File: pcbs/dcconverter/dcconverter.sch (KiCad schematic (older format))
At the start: 41 parts, among them IC1 NCP7805TG, J1 190-9991, J2 766-6629, J3 146-8335, J4 766-6604, J5 766-6604, Q1 NGTB40N120FL2WG, Q10 398-433, Q2 FQP47P06, Q3 2SK3747-1E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

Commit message: Cleanup Symbol Library
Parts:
- IC1: symbol SamacSys_Parts:NCP7805TG -> Custom:NCP7805TG
- L1: symbol dcconverter:2phase_inductor -> Custom:2phase_inductor
- Q2: symbol SamacSys_Parts:FQP47P06 -> Custom:FQP47P06
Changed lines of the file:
@@
 $EndComp
 $Comp
-L dcconverter:2phase_inductor L1
+L Custom:2phase_inductor L1
 U 1 1 5F94118A
 P 4000 2100
@@
 Connection ~ 1800 5750
 $Comp
-L SamacSys_Parts:FQP47P06 Q2
+L Custom:FQP47P06 Q2
 U 1 1 5F96B06C
 P 6700 2250
@@
 $EndComp
 $Comp
-L SamacSys_Parts:NCP7805TG IC1
+L Custom:NCP7805TG IC1
 U 1 1 5F9736CA
 P 3800 5150

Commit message: Cleanup Schematic
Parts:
- C1: footprint SamacSys_Parts:CAPPRD1250W100D2550H5200 -> Custom:CAPPRD1250W100D2550H5200
- J2: footprint SamacSys_Parts:CES-106-XX-Y-S -> Custom:CES-106-XX-Y-S
- J4, J5: footprint SamacSys_Parts:CES-102-XX-Y-S -> Custom:CES-102-XX-Y-S
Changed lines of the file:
@@
 F 0 "J2" H 1068 4117 50  0000 C CNN
 F 1 "766-6629" H 1068 4026 50  0000 C CNN
-F 2 "SamacSys_Parts:CES-106-XX-Y-S" H 1150 3700 50  0001 C CNN
+F 2 "Custom:CES-106-XX-Y-S" H 1150 3700 50  0001 C CNN
 F 3 "~" H 1150 3700 50  0001 C CNN
 	1    1150 3700
@@
 F 0 "C1" H 5168 2446 50  0000 L CNN
 F 1 "845-4749" H 5168 2355 50  0000 L CNN
-F 2 "SamacSys_Parts:CAPPRD1250W100D2550H5200" H 5088 2250 50  0001 C CNN
+F 2 "Custom:CAPPRD1250W100D2550H5200" H 5088 2250 50  0001 C CNN
 F 3 "~" H 5050 2400 50  0001 C CNN
 	1    5050 2400
@@
 F 0 "J4" H 1150 4600 50  0000 C CNN
 F 1 "766-6604" H 1150 4500 50  0000 C CNN
-F 2 "SamacSys_Parts:CES-102-XX-Y-S" H 1150 4350 50  0001 C CNN
+F 2 "Custom:CES-102-XX-Y-S" H 1150 4350 50  0001 C CNN
 F 3 "~" H 1150 4350 50  0001 C CNN
 	1    1150 4350
@@
 F 0 "J5" H 1150 5100 50  0000 C CNN
 F 1 "766-6604" H 1150 5000 50  0000 C CNN
-F 2 "SamacSys_Parts:CES-102-XX-Y-S" H 1150 4850 50  0001 C CNN
+F 2 "Custom:CES-102-XX-Y-S" H 1150 4850 50  0001 C CNN
 F 3 "~" H 1150 4850 50  0001 C CNN
 	1    1150 4850

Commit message: Update Footprints to use Custom PCB Library
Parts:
- J3: footprint dcconverter:connector_2pin_P10.6mm -> Custom:connector_2pin_P10.6mm
- L1: footprint dcconverter:rb8522_size5 -> Custom:rb8522_size5
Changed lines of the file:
@@
 F 0 "L1" H 4025 2515 50  0000 C CNN
 F 1 "769-0587" H 4025 2424 50  0000 C CNN
-F 2 "dcconverter:rb8522_size5" H 4000 2100 50  0001 C CNN
+F 2 "Custom:rb8522_size5" H 4000 2100 50  0001 C CNN
 F 3 "~" H 4000 2100 50  0001 C CNN
 	1    4000 2100
@@
 F 0 "J3" H 8680 1942 50  0000 L CNN
 F 1 "146-8335" H 8680 1851 50  0000 L CNN
-F 2 "dcconverter:connector_2pin_P10.6mm" H 8600 1950 50  0001 C CNN
+F 2 "Custom:connector_2pin_P10.6mm" H 8600 1950 50  0001 C CNN
 F 3 "~" H 8600 1950 50  0001 C CNN
 	1    8600 1950

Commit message: Use correct Symbol and Footprint Libraries
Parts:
- C1: symbol Device:CP -> Custom:CP-Device
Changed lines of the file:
@@
 Connection ~ 2900 1950
 $Comp
-L Device:CP C1
+L Custom:CP-Device C1
 U 1 1 5F94337F
 P 5050 2400

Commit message: Fix Heatsinks
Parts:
- HS-D1, HS-IC1, HS-Q1, HS-Q2: value 893-4942 -> HeatsinkUpright; footprint Heatsink:Heatsink_Fischer_SK129-STS_42x25mm_2xDrill2.5mm -> Custom:HeatsinkUpright
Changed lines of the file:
@@
 P 2450 1500
 F 0 "HS-Q1" H 2638 1539 50  0000 L CNN
-F 1 "893-4942" H 2638 1448 50  0000 L CNN
-F 2 "Heatsink:Heatsink_Fischer_SK129-STS_42x25mm_2xDrill2.5mm" H 2462 1450 50  0001 C CNN
+F 1 "HeatsinkUpright" H 2638 1448 50  0000 L CNN
+F 2 "Custom:HeatsinkUpright" H 2462 1450 50  0001 C CNN
 F 3 "~" H 2462 1450 50  0001 C CNN
 	1    2450 1500
@@
 P 2700 2700
 F 0 "HS-D1" V 2419 2693 50  0000 C CNN
-F 1 "893-4942" V 2510 2693 50  0000 C CNN
-F 2 "Heatsink:Heatsink_Fischer_SK129-STS_42x25mm_2xDrill2.5mm" H 2712 2650 50  0001 C CNN
+F 1 "HeatsinkUpright" V 2510 2693 50  0000 C CNN
+F 2 "Custom:HeatsinkUpright" H 2712 2650 50  0001 C CNN
 F 3 "~" H 2712 2650 50  0001 C CNN
 	1    2700 2700
@@
 P 6800 1500
 F 0 "HS-Q2" H 6988 1539 50  0000 L CNN
-F 1 "893-4942" H 6988 1448 50  0000 L CNN
-F 2 "Heatsink:Heatsink_Fischer_SK129-STS_42x25mm_2xDrill2.5mm" H 6812 1450 50  0001 C CNN
+F 1 "HeatsinkUpright" H 6988 1448 50  0000 L CNN
+F 2 "Custom:HeatsinkUpright" H 6812 1450 50  0001 C CNN
 F 3 "~" H 6812 1450 50  0001 C CNN
 	1    6800 1500
@@
 P 4300 4900
 F 0 "HS-IC1" H 4488 4939 50  0000 L CNN
-F 1 "893-4942" H 4488 4848 50  0000 L CNN
-F 2 "Heatsink:Heatsink_Fischer_SK129-STS_42x25mm_2xDrill2.5mm" H 4312 4850 50  0001 C CNN
+F 1 "HeatsinkUpright" H 4488 4848 50  0000 L CNN
+F 2 "Custom:HeatsinkUpright" H 4312 4850 50  0001 C CNN
 F 3 "~" H 4312 4850 50  0001 C CNN
 	1    4300 4900

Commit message: Fix Footprint for J1
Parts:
- J1: footprint TerminalBlock_Dinkle:TerminalBlock_Dinkle_DT-55-B01X-02_P10.00mm -> Custom:TerminalBlock_2pin_10mm
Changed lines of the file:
@@
 F 0 "J1" H 1168 2167 50  0000 C CNN
 F 1 "190-9991" H 1168 2076 50  0000 C CNN
-F 2 "TerminalBlock_Dinkle:TerminalBlock_Dinkle_DT-55-B01X-02_P10.00mm" H 1250 1950 50  0001 C CNN
+F 2 "Custom:TerminalBlock_2pin_10mm" H 1250 1950 50  0001 C CNN
 F 3 "~" H 1250 1950 50  0001 C CNN
 	1    1250 1950

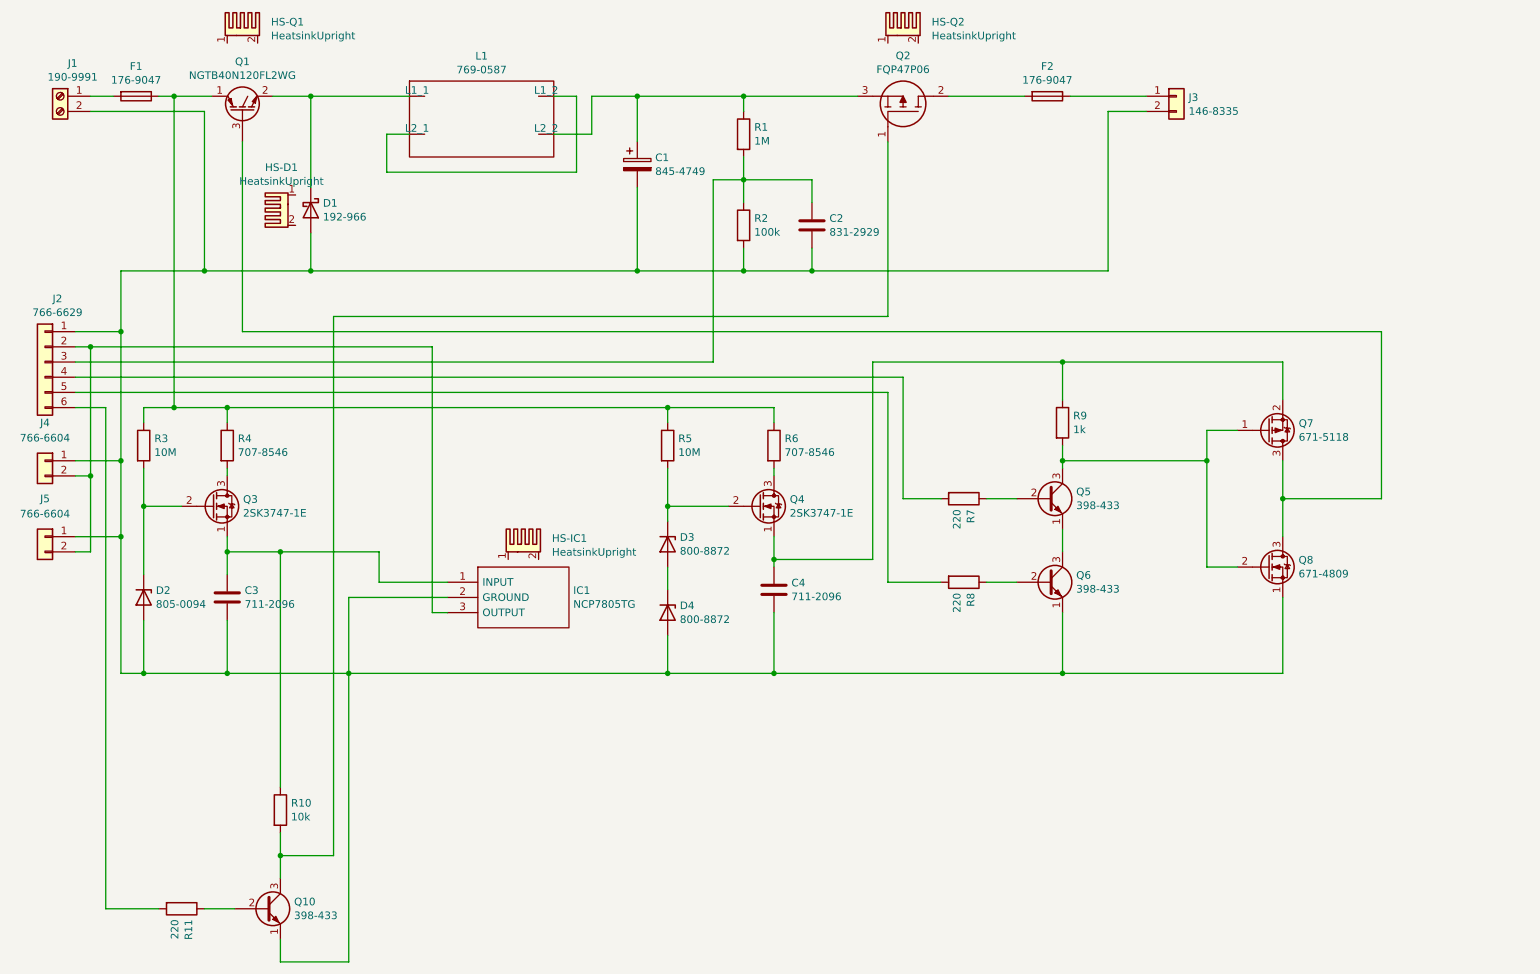
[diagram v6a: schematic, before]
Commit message: Fix Issues with Voltage Source in DC DC Converter
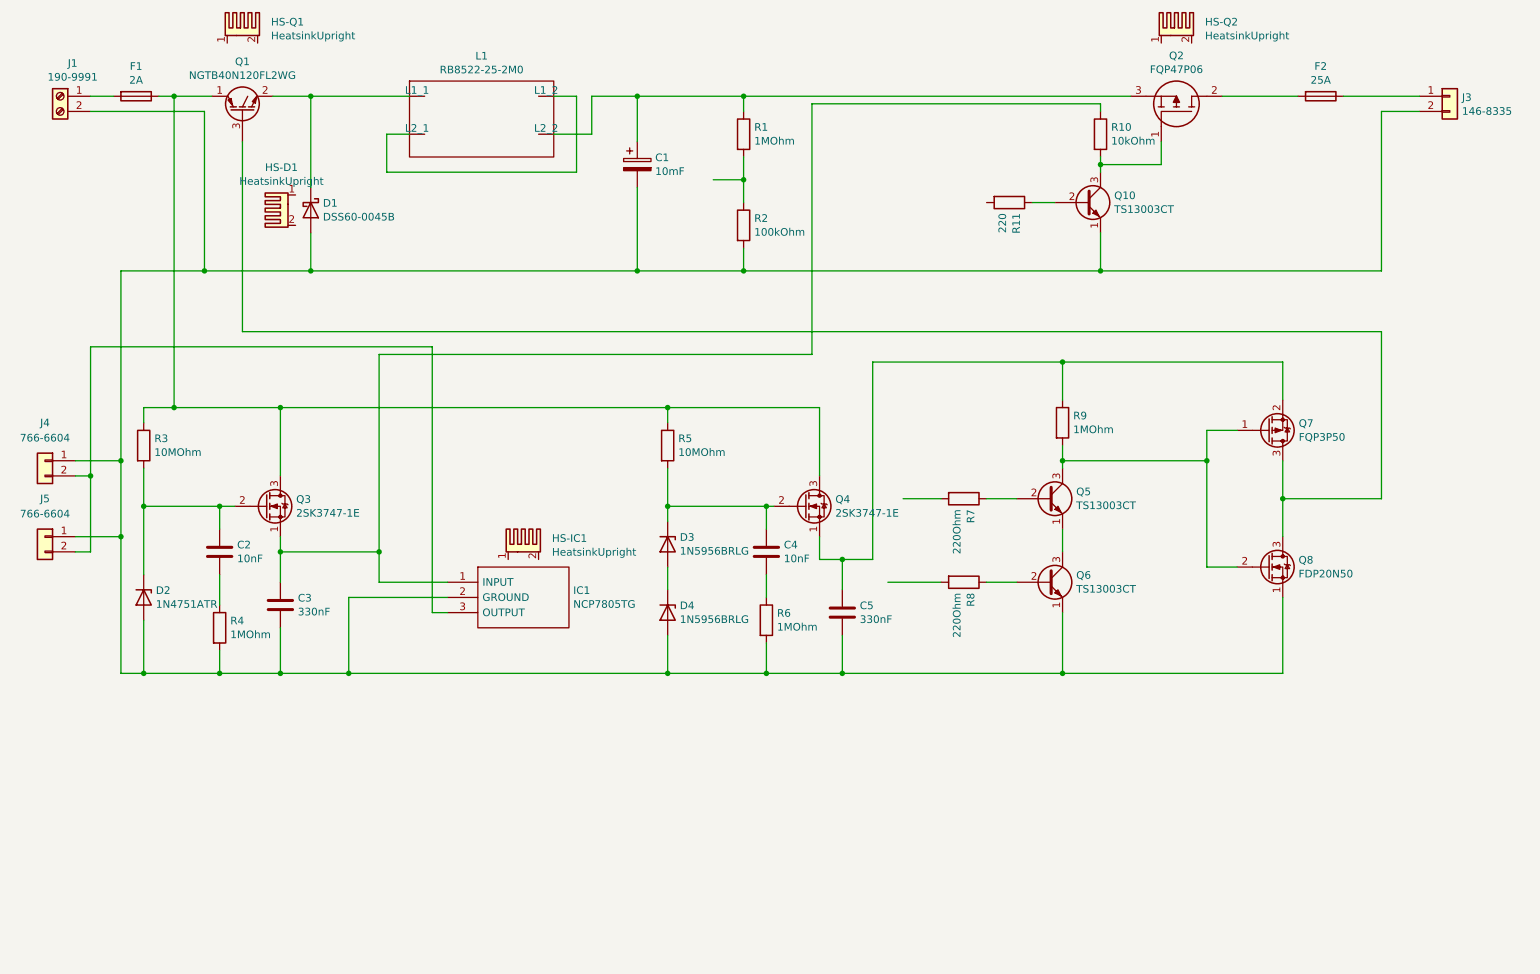
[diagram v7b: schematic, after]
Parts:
- removed J2: 766-6629, Custom:CES-106-XX-Y-S, symbol Connector_Generic:Conn_01x06
- added C5: 330nF, symbol Device:C
- C1: value 845-4749 -> 10mF
- C2: value 831-2929 -> 10nF; footprint Capacitor_THT:C_Disc_D7.5mm_W5.0mm_P7.50mm -> (none)
- C3: value 711-2096 -> 330nF; footprint Capacitor_THT:CP_Radial_D18.0mm_P7.50mm -> (none)
- C4: value 711-2096 -> 10nF; footprint Capacitor_THT:CP_Radial_D18.0mm_P7.50mm -> (none)
- D1: value 192-966 -> DSS60-0045B
- D2: value 805-0094 -> 1N4751ATR
- D3, D4: value 800-8872 -> 1N5956BRLG
- F1: value 176-9047 -> 2A
- F2: value 176-9047 -> 25A
- L1: value 769-0587 -> RB8522-25-2M0
- Q10, Q5, Q6: value 398-433 -> TS13003CT
- Q7: value 671-5118 -> FQP3P50
- Q8: value 671-4809 -> FDP20N50
- R1: value 1M -> 1MOhm
- R10: value 10k -> 10kOhm
- R2: value 100k -> 100kOhm
- R3, R5: value 10M -> 10MOhm
- R4, R6: value 707-8546 -> 1MOhm
- R7, R8: value 220 -> 220Ohm
- R9: value 1k -> 1MOhm
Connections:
- net at C1.2, C3.2, D1.2 (A)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: now also R4.2, R6.2, C5.2; no longer C2.2, C4.2
- net at F1.1, Q1.1 (C), R3.1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: now also Q3.3 (D), Q4.3 (D); no longer R4.1, R6.1
- net at R1.2, R2.1: no longer C2.1
- net at D2.1 (K), Q3.2 (G), R3.2: now also C2.1
- net at D3.1 (K), Q4.2 (G), R5.2: now also C4.1
- net at Q4.1 (S), Q7.2 (S), R9.1: now also C5.1; no longer C4.1
- new net: C2.2, R4.1
- new net: C4.2, R6.1
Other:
- moved on the sheet: F2, HS-Q2, J3, Q10, Q2, Q3, Q4, R10, R11

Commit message: Use correct footprint for Q10
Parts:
- Q10: footprint Package_TO_SOT_THT:TO-92_Inline -> Custom:TS13003CT_wide
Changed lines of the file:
@@
 F 0 "Q10" H 8190 2696 50  0000 L CNN
 F 1 "TS13003CT" H 8190 2605 50  0000 L CNN
-F 2 "Package_TO_SOT_THT:TO-92_Inline" H 8200 2575 50  0001 L CIN
+F 2 "Custom:TS13003CT_wide" H 8200 2575 50  0001 L CIN
 F 3 "" H 8000 2650 50  0001 L CNN
 	1    8000 2650
